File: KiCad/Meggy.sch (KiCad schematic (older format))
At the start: 24 parts, among them J1 USB_B_Micro, J2 Conn_01x03, Q1 DMP2305U-7, Q2 DMP2305U-7, Q3 DMP2305U-7, U1 ROM-socket-42pin, U2 AT90USB1286-MU, U3 M29F160F, X1 Standard_Clock_Oscillators_XT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

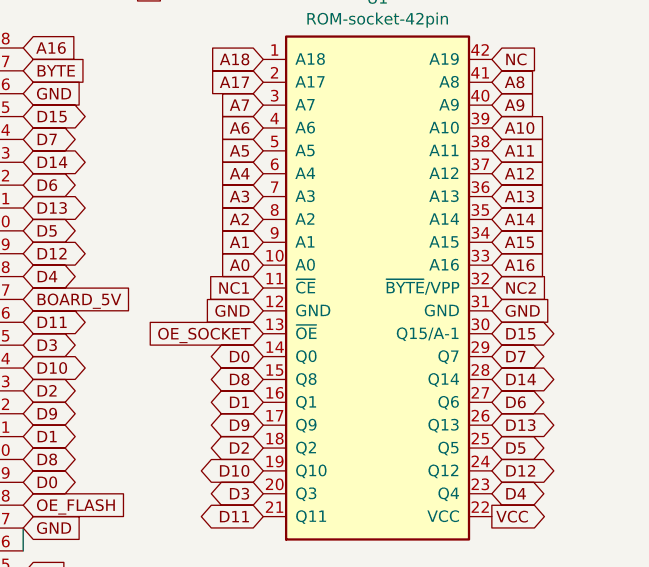
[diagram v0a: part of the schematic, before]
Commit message: Add GND via stitching and some improved routing
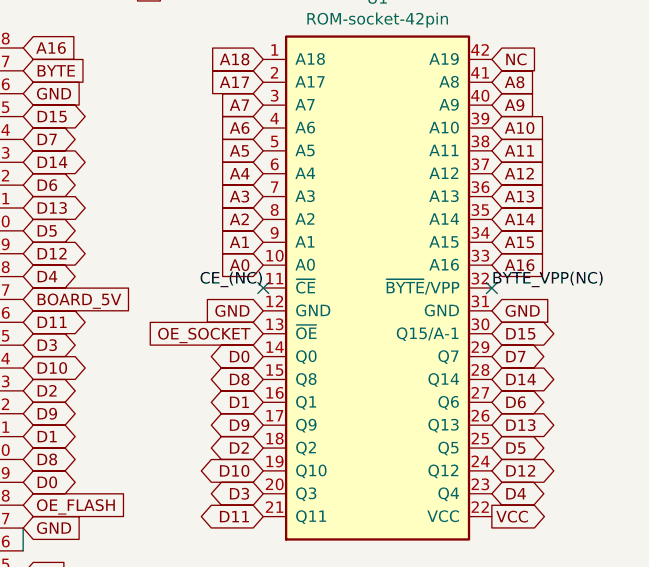
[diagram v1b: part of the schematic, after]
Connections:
- net NC1 renamed CE_(NC)
- net NC2 renamed BYTE_VPP(NC)
- no-connect marks 2 -> 4
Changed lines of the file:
@@
 Text GLabel 7900 3550 2    50   Input ~ 0
 GND
-Text GLabel 7900 3450 2    50   Input ~ 0
-NC2
 Text GLabel 3050 6250 3    50   Input ~ 0
 GND
@@
 Text GLabel 7900 3650 2    50   BiDi ~ 0
 D15
-Text GLabel 6900 3450 0    50   Input ~ 0
-NC1
 Wire Wire Line
 	5850 4500 5850 4600
@@
 Text GLabel 7500 1100 3    50   Input ~ 0
 RST
+NoConn ~ 6900 3450
+Text Label 6900 3450 2    50   ~ 0
+CE_(NC)
+Text Label 7900 3450 0    50   ~ 0
+BYTE_VPP(NC)
+NoConn ~ 7900 3450
 $EndSCHEMATC

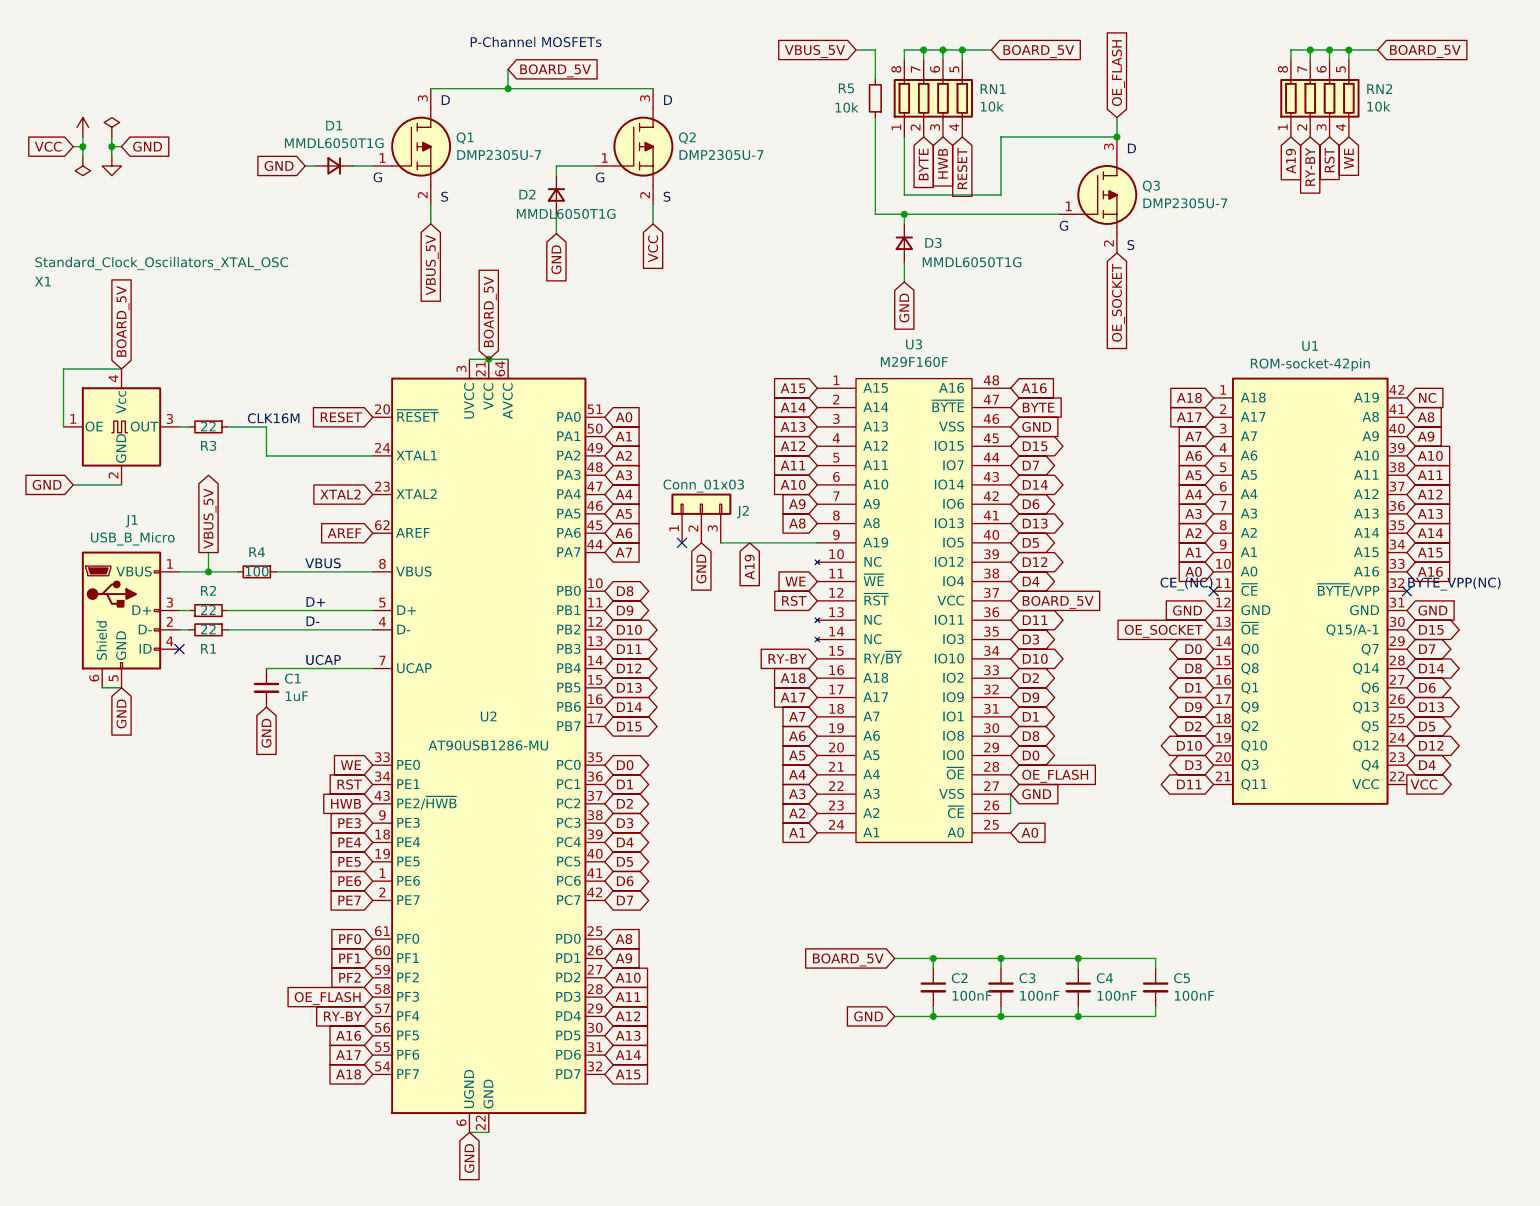
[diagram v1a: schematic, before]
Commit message: Add push button for RESET and HWB lines
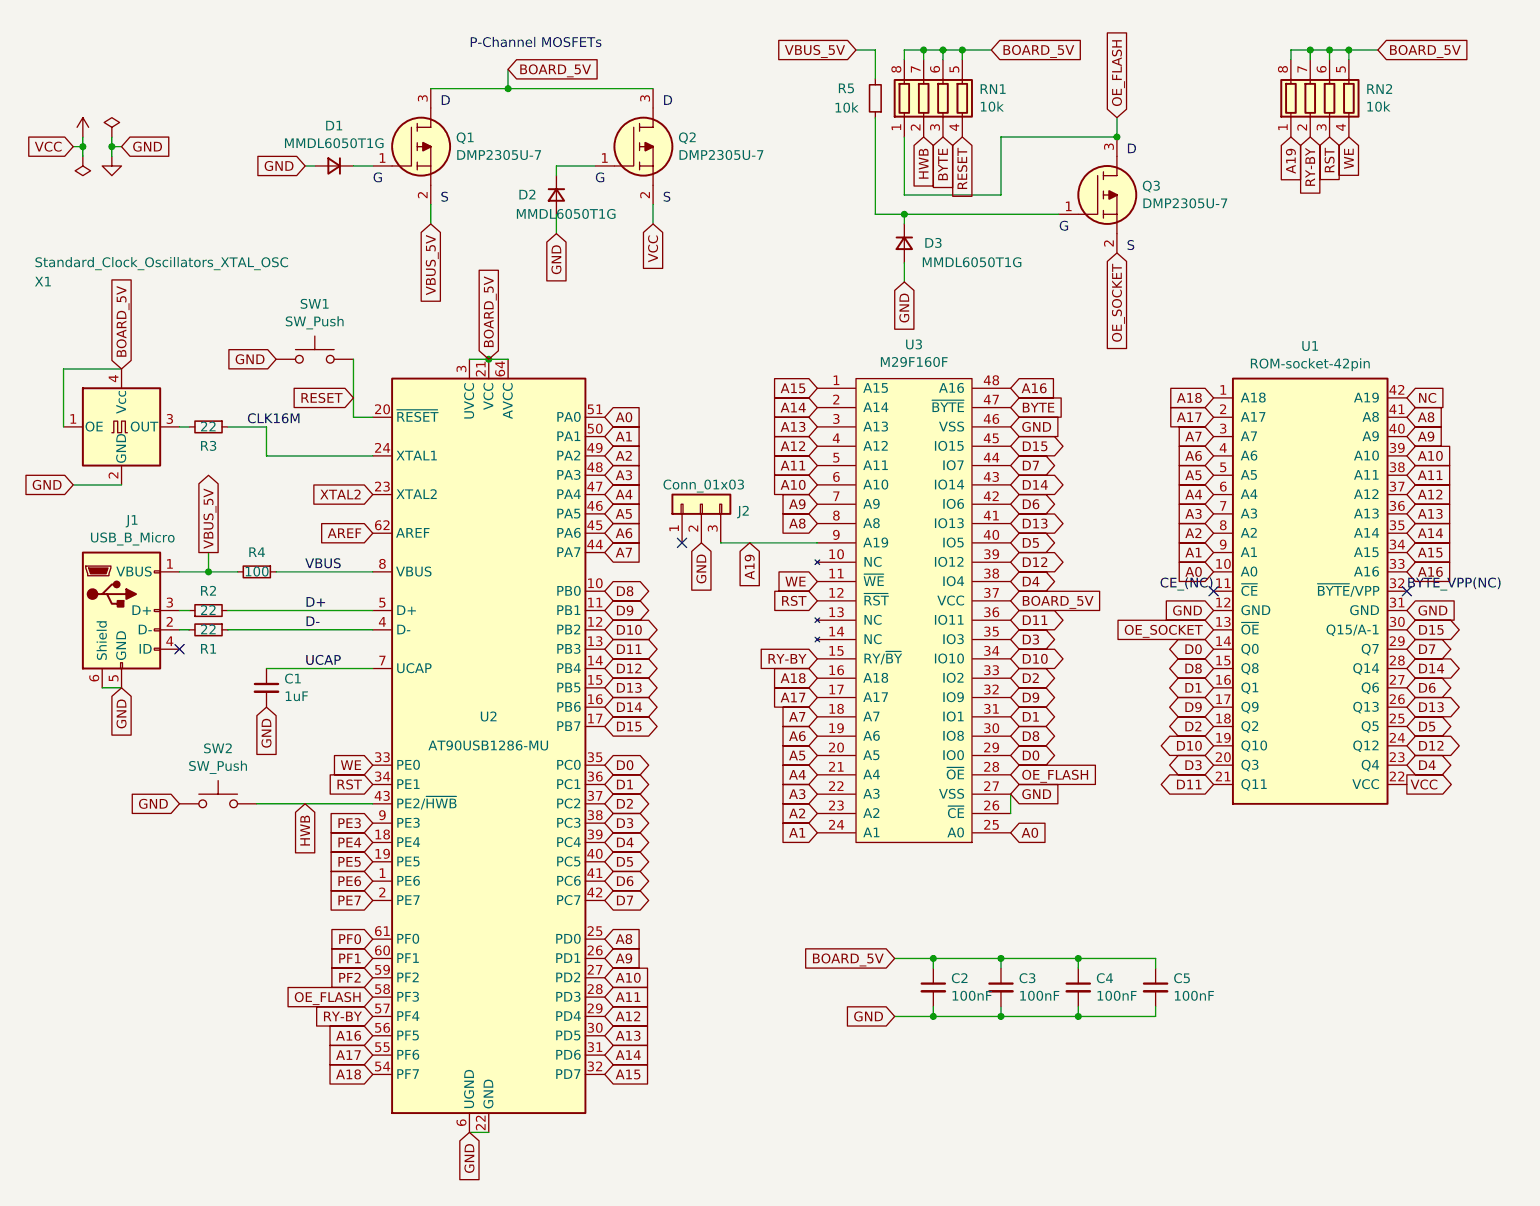
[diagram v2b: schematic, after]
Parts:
- added SW1, SW2: SW_Push, Meggy:Sunrom_Tactile_Switch_3x4x2mm_SMD_2-Pin, symbol Switch:SW_Push
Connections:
- net BYTE: now also RN1.3 (R3.1); no longer RN1.2 (R2.1)
- net GND: now also SW1.1, SW2.1
- net HWB: now also RN1.2 (R2.1), SW2.2; no longer RN1.3 (R3.1)
- net RESET: now also SW1.2
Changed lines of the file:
@@
 Text GLabel 2550 2950 0    50   Input ~ 0
 XTAL2
-Text GLabel 2550 2550 0    50   Input ~ 0
+Text GLabel 2450 2450 0    50   Input ~ 0
 RESET
 Text GLabel 2550 3150 0    50   Input ~ 0
 AREF
-Text GLabel 2550 4550 0    50   Input ~ 0
+Text GLabel 2200 4550 3    50   Input ~ 0
 HWB
 Text GLabel 2550 4650 0    50   Input ~ 0
@@
 Text GLabel 5600 1100 3    50   Input ~ 0
 RESET
-Text GLabel 5500 1100 3    50   Input ~ 0
-HWB
 Text GLabel 5050 650  0    50   Input ~ 0
 VBUS_5V
@@
 	5300 650  5300 700
 Connection ~ 5400 650
-Text GLabel 5400 1100 3    50   Input ~ 0
-BYTE
 $Comp
 L Device:R_Small R5
@@
 BYTE_VPP(NC)
 NoConn ~ 7900 3450
+$Comp
+L Switch:SW_Push SW1
+U 1 1 68D03EF3
+P 2250 2250
+F 0 "SW1" H 2250 2535 50  0000 C CNN
+F 1 "SW_Push" H 2250 2444 50  0000 C CNN
+F 2 "Meggy:Sunrom_Tactile_Switch_3x4x2mm_SMD_2-Pin" H 2250 2450 50  0001 C CNN
+F 3 "~" H 2250 2450 50  0001 C CNN
+	1    2250 2250
+	1    0    0    -1
+$EndComp
+Text GLabel 2050 2250 0    50   Input ~ 0
+GND
+Wire Wire Line
+	2550 2550 2450 2550
+Wire Wire Line
+	2450 2550 2450 2250
+$Comp
+L Switch:SW_Push SW2
+U 1 1 68D65985
+P 1750 4550
+F 0 "SW2" H 1750 4835 50  0000 C CNN
+F 1 "SW_Push" H 1750 4744 50  0000 C CNN
+F 2 "Meggy:Sunrom_Tactile_Switch_3x4x2mm_SMD_2-Pin" H 1750 4750 50  0001 C CNN
+F 3 "~" H 1750 4750 50  0001 C CNN
+	1    1750 4550
+	1    0    0    -1
+$EndComp
+Text GLabel 1550 4550 0    50   Input ~ 0
+GND
+Wire Wire Line
+	1950 4550 2550 4550
+Text GLabel 5500 1100 3    50   Input ~ 0
+BYTE
+Text GLabel 5400 1100 3    50   Input ~ 0
+HWB
 $EndSCHEMATC

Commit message: Add 3D model for push buttons and fix names on pads not used (NC)
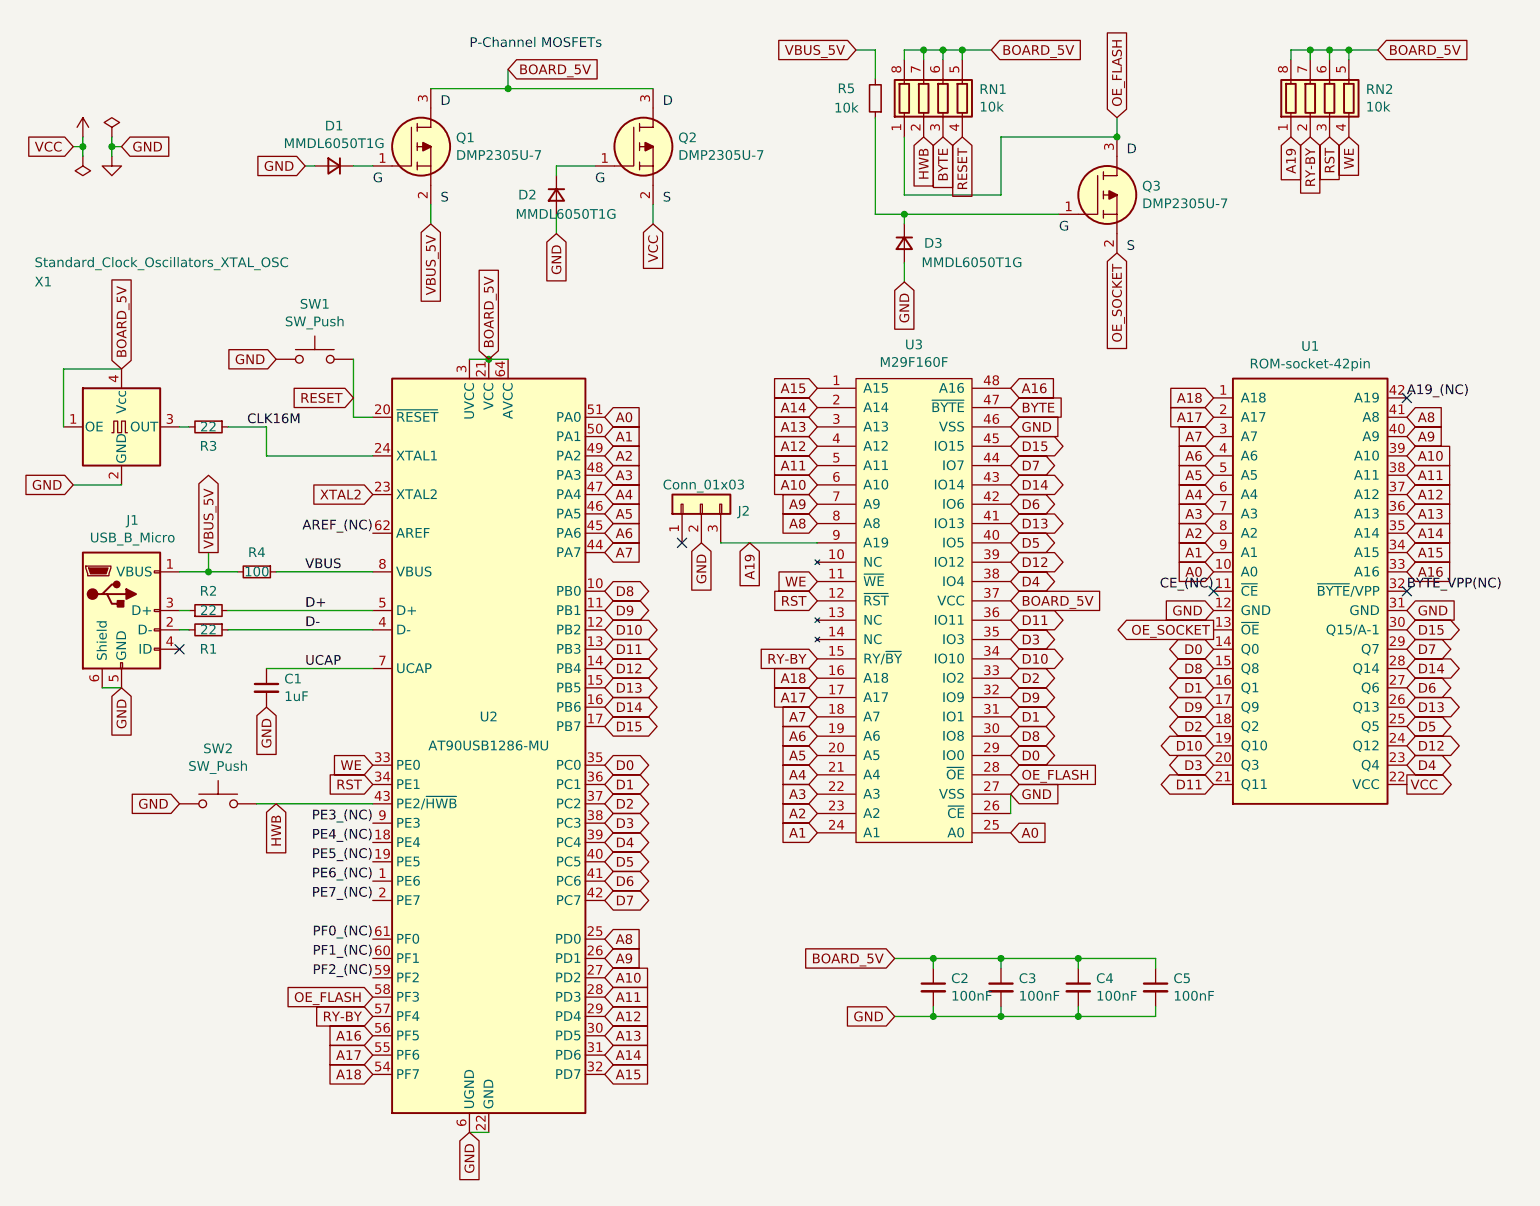
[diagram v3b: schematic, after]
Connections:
- net AREF renamed AREF_(NC)
- net NC renamed A19_(NC)
- net PE3 renamed PE3_(NC)
- net PE4 renamed PE4_(NC)
- net PE5 renamed PE5_(NC)
- net PE6 renamed PE6_(NC)
- net PE7 renamed PE7_(NC)
- net PF0 renamed PF0_(NC)
- net PF1 renamed PF1_(NC)
- net PF2 renamed PF2_(NC)
- no-connect marks 4 -> 5
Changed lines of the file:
@@
 Text GLabel 3050 6250 3    50   Input ~ 0
 GND
-Text GLabel 7900 2450 2    50   Input ~ 0
-NC
 $Comp
 L Meggy:M29F160F U3
@@
 Text GLabel 2450 2450 0    50   Input ~ 0
 RESET
-Text GLabel 2550 3150 0    50   Input ~ 0
-AREF
-Text GLabel 2200 4550 3    50   Input ~ 0
+Text GLabel 2050 4550 3    50   Input ~ 0
 HWB
-Text GLabel 2550 4650 0    50   Input ~ 0
-PE3
-Text GLabel 2550 4750 0    50   Input ~ 0
-PE4
-Text GLabel 2550 5250 0    50   Input ~ 0
-PF0
-Text GLabel 2550 5350 0    50   Input ~ 0
-PF1
-Text GLabel 2550 5450 0    50   Input ~ 0
-PF2
-Text GLabel 2550 4850 0    50   Input ~ 0
-PE5
-Text GLabel 2550 4950 0    50   Input ~ 0
-PE6
-Text GLabel 2550 5050 0    50   Input ~ 0
-PE7
 Text GLabel 4850 3400 0    50   Input ~ 0
 WE
@@
 Text GLabel 6400 1700 3    50   Input ~ 0
 OE_SOCKET
-Text GLabel 6900 3650 0    50   Input ~ 0
+Text GLabel 6900 3650 0    50   Output ~ 0
 OE_SOCKET
 $Comp
@@
 Text GLabel 5400 1100 3    50   Input ~ 0
 HWB
+NoConn ~ 7900 2450
+Text Label 7900 2450 0    50   ~ 0
+A19_(NC)
+Text Label 2550 3150 2    50   ~ 0
+AREF_(NC)
+Text Label 2550 4650 2    50   ~ 0
+PE3_(NC)
+Text Label 2550 4750 2    50   ~ 0
+PE4_(NC)
+Text Label 2550 4850 2    50   ~ 0
+PE5_(NC)
+Text Label 2550 4950 2    50   ~ 0
+PE6_(NC)
+Text Label 2550 5050 2    50   ~ 0
+PE7_(NC)
+Text Label 2550 5250 2    50   ~ 0
+PF0_(NC)
+Text Label 2550 5350 2    50   ~ 0
+PF1_(NC)
+Text Label 2550 5450 2    50   ~ 0
+PF2_(NC)
 $EndSCHEMATC

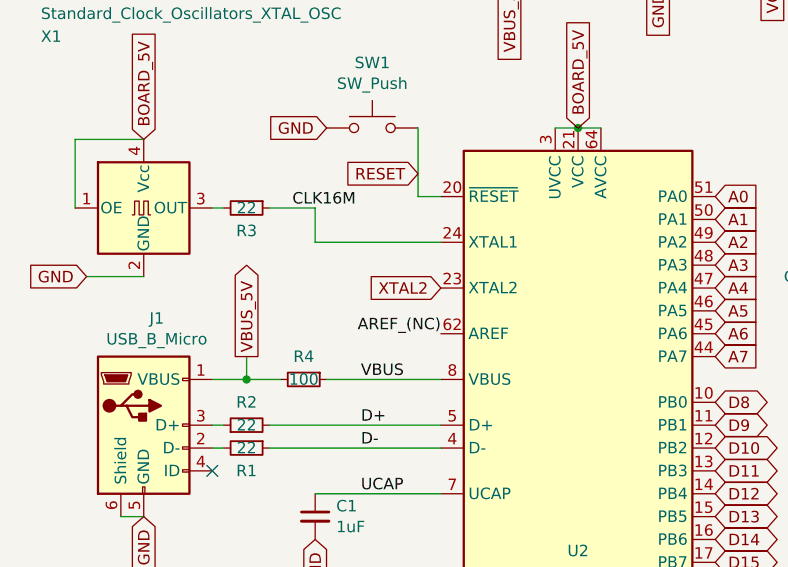
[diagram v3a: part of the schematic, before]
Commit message: Moving into 6-layer PCB design
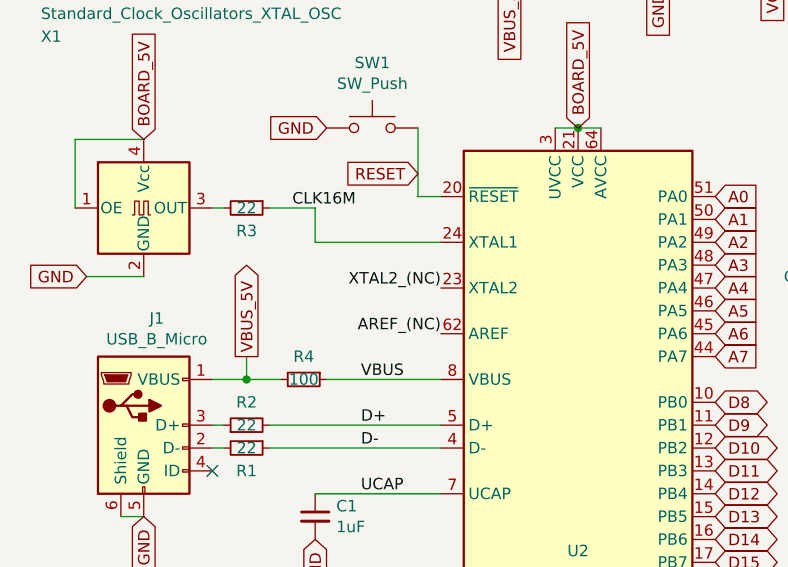
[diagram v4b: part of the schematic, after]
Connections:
- net XTAL2 renamed XTAL2_(NC)
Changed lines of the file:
@@
 Text GLabel 2550 5950 0    50   Input ~ 0
 A18
-Text GLabel 2550 2950 0    50   Input ~ 0
-XTAL2
 Text GLabel 2450 2450 0    50   Input ~ 0
 RESET
@@
 Text Label 2550 5450 2    50   ~ 0
 PF2_(NC)
+Text Label 2550 2950 2    50   ~ 0
+XTAL2_(NC)
 $EndSCHEMATC
